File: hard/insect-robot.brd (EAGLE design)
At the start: 10.2 x 25.4 mm, 12 parts, among them SW1 SWITCH-DT, U1 ATMEGA328P-QFN32, U2 PW0316

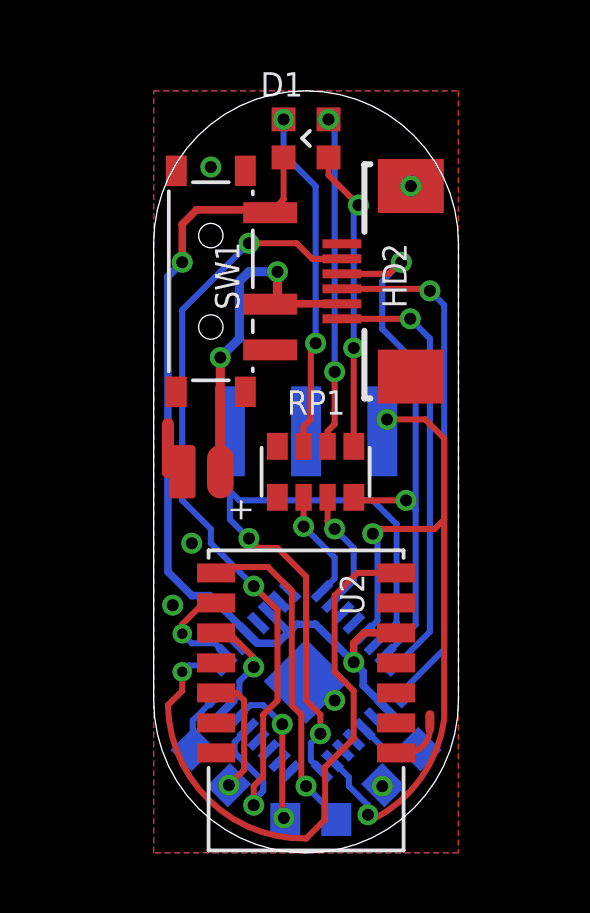
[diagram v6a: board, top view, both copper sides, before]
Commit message: Remove non-PWM elctrode pins
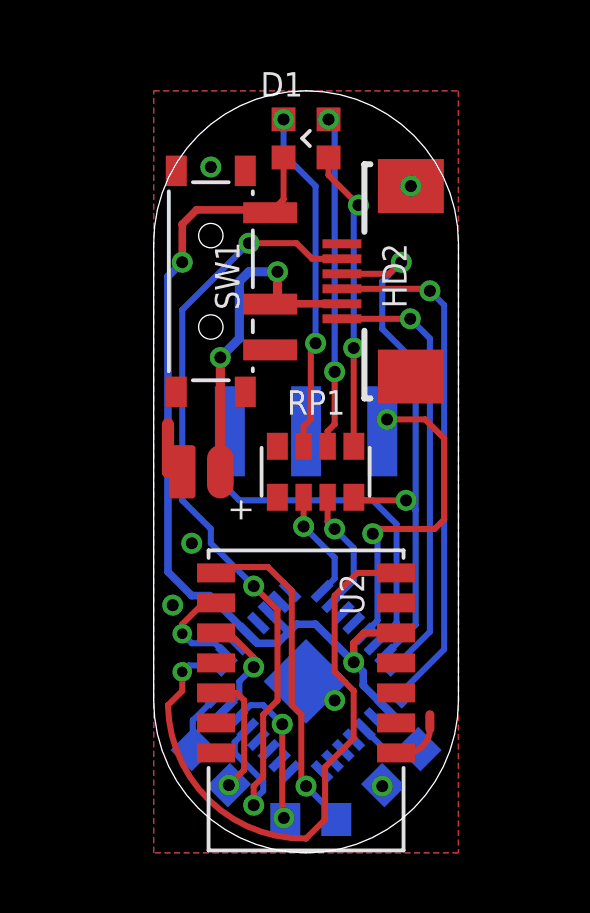
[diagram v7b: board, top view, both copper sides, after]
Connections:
- net L: no longer U1.24
- net R: no longer U1.23
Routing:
- net R: track 24.8 -> 11.5 mm, vias 3 -> 2
- net L: track 23.6 -> 12.3 mm, vias 2 -> 0
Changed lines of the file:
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@@
 <signal name="L">
 <contactref element="HD1" pad="1"/>
-<contactref element="U1" pad="24"/>
 <wire x1="2.54" y1="12.065" x2="2.54" y2="14.05" width="0.2032" layer="16"/>
-<via x="5.55625" y="3.96875" extent="1-16" drill="0.4"/>
-<wire x1="5.55625" y1="4.60375" x2="5.08" y2="5.08" width="0.2032" layer="1"/>
-<wire x1="5.55625" y1="4.60375" x2="5.55625" y2="3.96875" width="0.2032" layer="1"/>
-<wire x1="5.55625" y1="3.96875" x2="5.23875" y2="3.65125" width="0.2032" layer="16"/>
-<wire x1="5.23875" y1="3.65125" x2="5.23875" y2="3.081375" width="0.2032" layer="16"/>
-<wire x1="5.23875" y1="3.081375" x2="5.61033125" y2="2.70979375" width="0.2032" layer="16"/>
 <contactref element="U1" pad="14"/>
 <wire x1="7.3781" y1="6.952434375" x2="8.09625" y2="7.670584375" width="0.2032" layer="16"/>
 <wire x1="7.3025" y1="11.7475" x2="2.8575" y2="11.7475" width="0.2032" layer="16"/>
 <wire x1="2.8575" y1="11.7475" x2="2.54" y2="12.065" width="0.2032" layer="16"/>
-<wire x1="5.08" y1="5.08" x2="5.08" y2="9.2075" width="0.2032" layer="1"/>
-<wire x1="5.08" y1="9.2075" x2="4.1275" y2="10.16" width="0.2032" layer="1"/>
-<wire x1="4.1275" y1="10.16" x2="3.4925" y2="10.16" width="0.2032" layer="1"/>
-<wire x1="3.4925" y1="10.16" x2="3.175" y2="10.4775" width="0.2032" layer="1"/>
-<via x="3.175" y="10.4775" extent="1-16" drill="0.4"/>
-<wire x1="3.175" y1="10.4775" x2="2.54" y2="11.1125" width="0.2032" layer="16"/>
-<wire x1="2.54" y1="11.1125" x2="2.54" y2="12.065" width="0.2032" layer="16"/>
 <wire x1="8.09625" y1="7.670584375" x2="8.09625" y2="10.95375" width="0.2032" layer="16"/>
 <wire x1="8.09625" y1="10.95375" x2="7.3025" y2="11.7475" width="0.2032" layer="16"/>
@@
 <signal name="R">
 <contactref element="HD1" pad="3"/>
-<contactref element="U1" pad="23"/>
-<wire x1="9.68375" y1="4.445" x2="7.3025" y2="1.11125" width="0.2032" layer="1" curve="-55.715945"/>
-<wire x1="7.3025" y1="1.11125" x2="7.14375" y2="1.27" width="0.2032" layer="1"/>
-<via x="7.14375" y="1.27" extent="1-16" drill="0.4"/>
-<wire x1="7.14375" y1="1.27" x2="7.14375" y2="1.5875" width="0.2032" layer="16"/>
-<wire x1="7.14375" y1="1.5875" x2="6.50875" y2="2.2225" width="0.2032" layer="16"/>
-<wire x1="6.50875" y1="2.2225" x2="6.50875" y2="2.51848125" width="0.2032" layer="16"/>
-<wire x1="6.50875" y1="2.51848125" x2="5.963884375" y2="3.063346875" width="0.2032" layer="16"/>
 <via x="7.77875" y="14.44625" extent="1-16" drill="0.4"/>
-<wire x1="9.68375" y1="4.445" x2="9.68375" y2="11.1125" width="0.2032" layer="1"/>
 <wire x1="9.68375" y1="11.1125" x2="9.68375" y2="13.81125" width="0.2032" layer="1"/>
 <wire x1="9.68375" y1="13.81125" x2="9.04875" y2="14.44625" width="0.2032" layer="1"/>
